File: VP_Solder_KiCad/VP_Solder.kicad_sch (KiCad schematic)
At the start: 159 parts, among them J1 Conn_01x04, SW1 SW_Push, SW2 SW_Push, U1 STM32F072CBTx, U2 XC6206PxxxMR, U3 USBLC6-2SC6

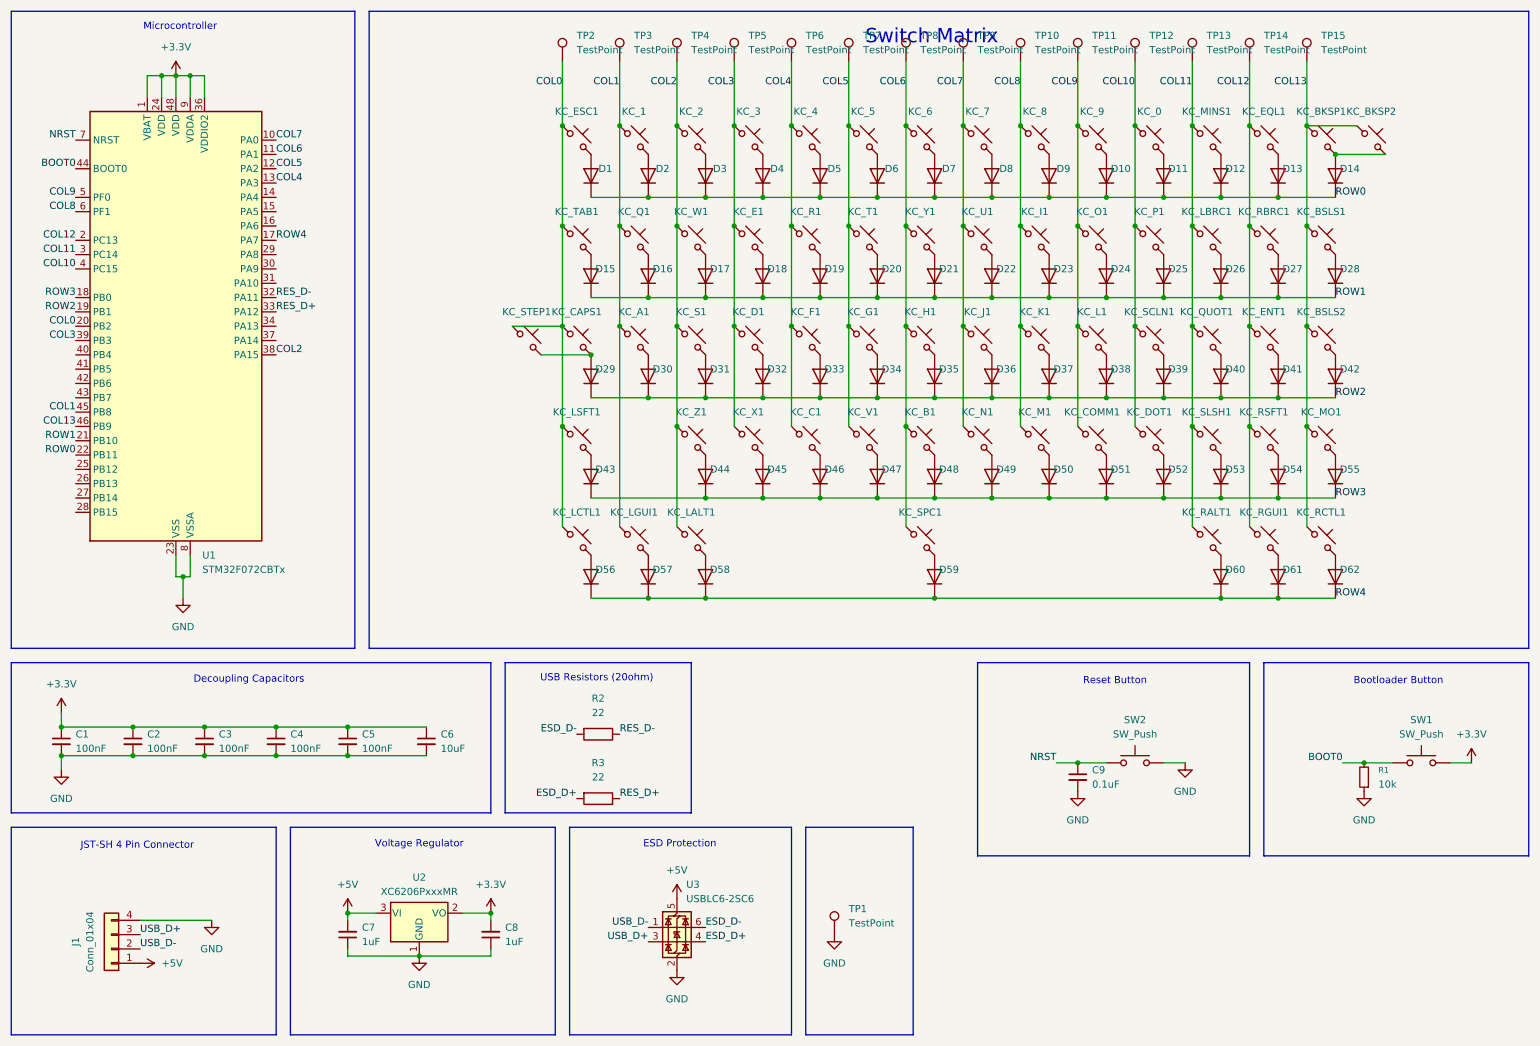
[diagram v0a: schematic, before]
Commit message: Changed testpoint names
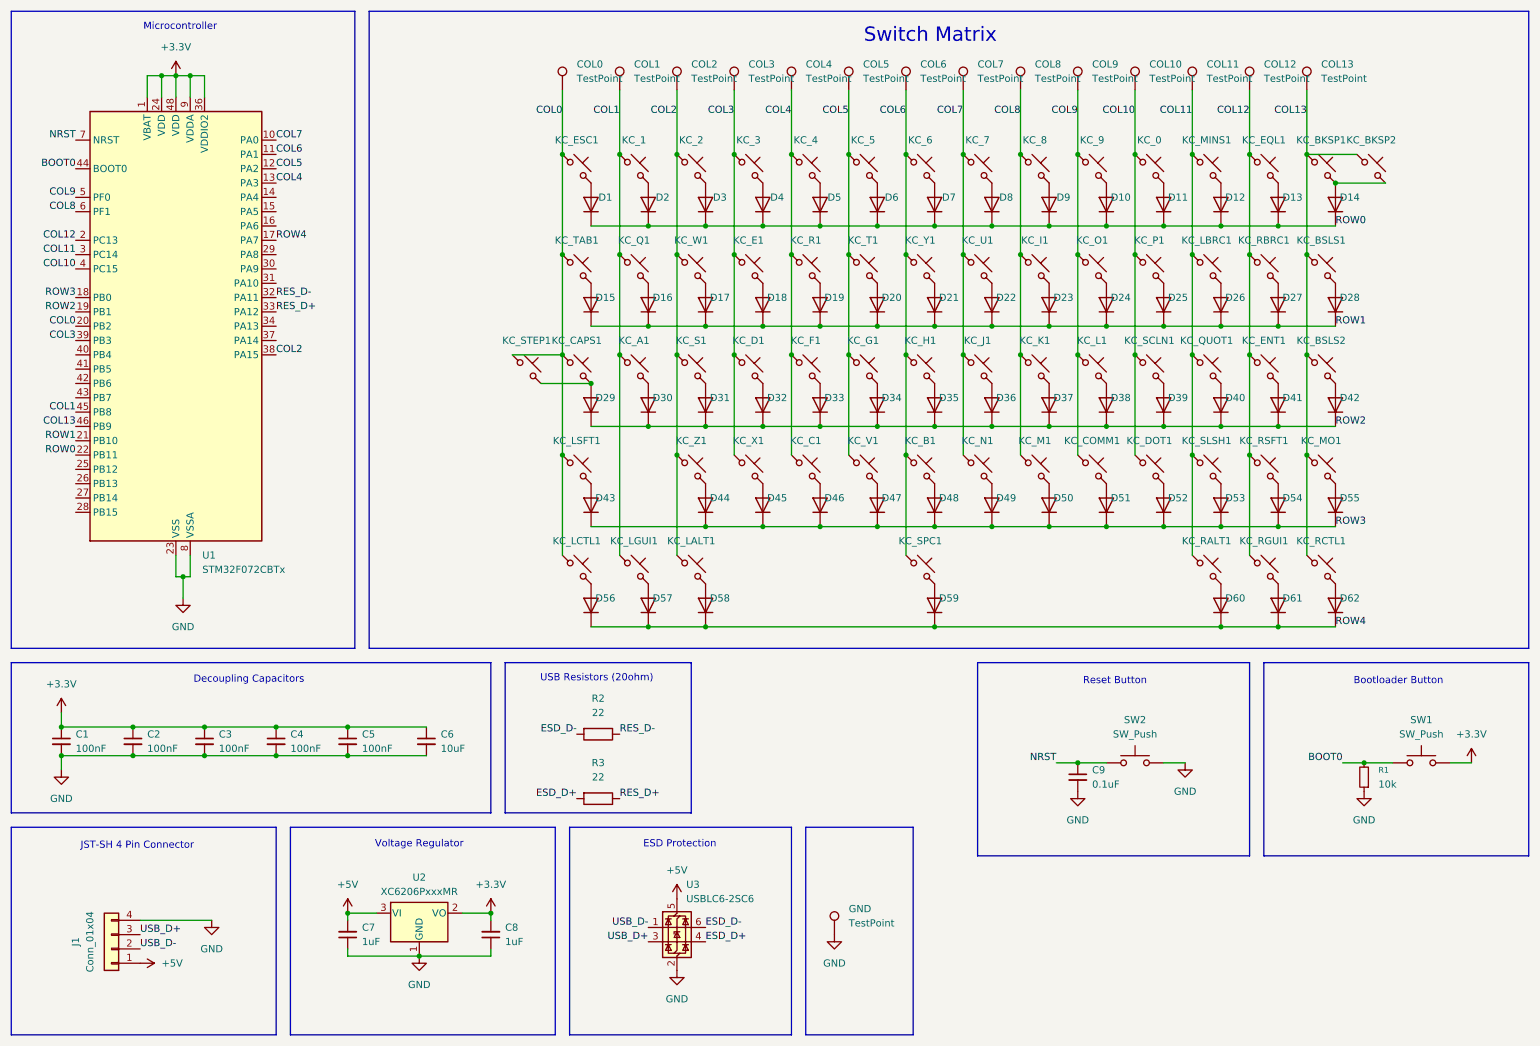
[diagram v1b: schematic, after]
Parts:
- renumbered TP2 to COL0, TP3 to COL1, TP12 to COL10, TP13 to COL11, TP14 to COL12, TP15 to COL13, TP4 to COL2, TP5 to COL3, TP6 to COL4, TP7 to COL5, TP8 to COL6, TP9 to COL7, TP10 to COL8, TP11 to COL9, TP1 to GND
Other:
- moved on the sheet: COL0, COL1, COL10, COL11, COL12, COL13, COL2, COL3, COL4, COL5, COL6, COL7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

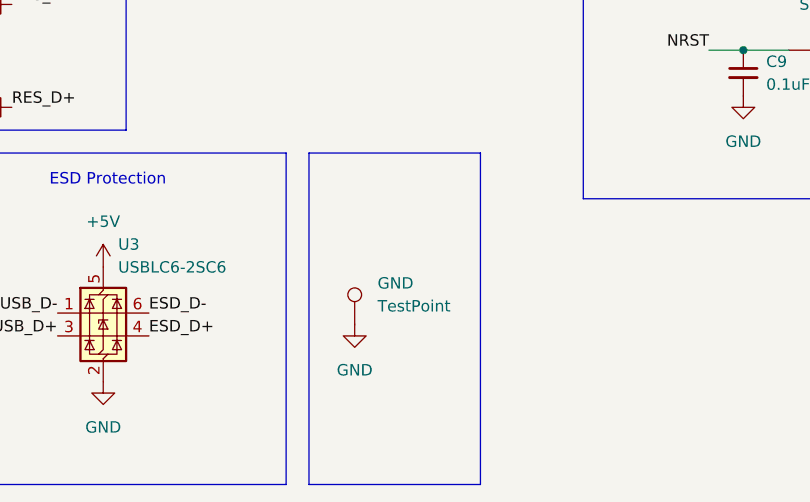
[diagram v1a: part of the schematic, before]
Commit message: Changed silkscreen
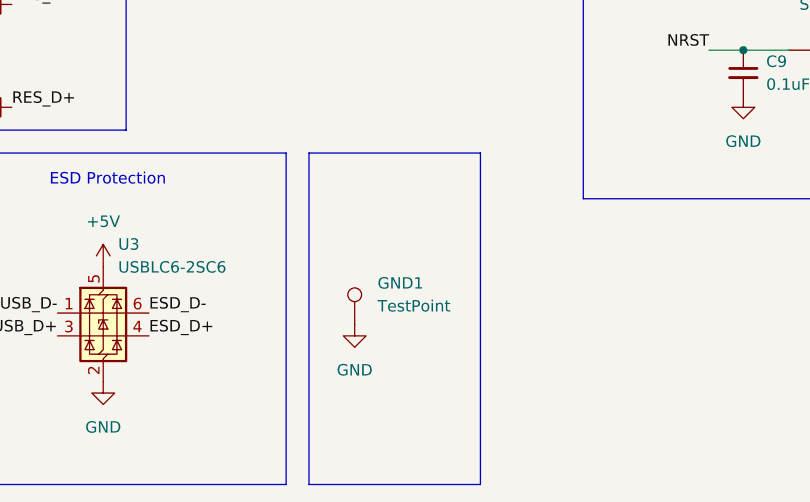
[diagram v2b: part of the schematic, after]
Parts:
- renumbered GND to GND1
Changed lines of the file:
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@@
 		(dnp no)
 		(fields_autoplaced yes)
-		(property "Reference" "GND"
+		(property "Reference" "GND1"
 			(at 162.56 173.2279 0)
 			(show_name no)
@@
 			(project "VP_Solder"
 				(path "/e464f1d1-4c01-4fad-a203-20008a0f30b7"
-					(reference "GND")
+					(reference "GND1")
 					(unit 1)
 				)

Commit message: final changes, drc fixes
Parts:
- removed R2, R3: 22, Resistor_SMD:R_0201_0603Metric, symbol Device:R
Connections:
- net RES_D+ is gone; now on net ESD_D+: U1.33 (PA12)
- net RES_D- is gone; now on net ESD_D-: U1.32 (PA11)
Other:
- note removed: "USB Resistors (20ohm)"
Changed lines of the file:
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@@
 	)
 	(rectangle
-		(start 101.6 129.54)
-		(end 134.62 156.21)
-		(stroke
-			(width 0)
-			(type default)
-		)
-		(fill
-			(type none)
-		)
-	)
-	(rectangle
 		(start 113.03 158.75)
 		(end 152.4 195.58)
@@
 		)
 	)
-	(text "USB Resistors (20ohm)"
-		(exclude_from_sim no)
-		(at 117.856 132.334 0)
-		(effects
-			(font
-				(size 1.27 1.27)
-			)
-		)
-	)
 	(junction
 		(at 147.32 69.85)
@@
 		)
 	)
-	(label "ESD_D+"
-		(at 114.3 153.67 180)
+	(label "ESD_D-"
+		(at 60.96 64.77 0)
 		(effects
 			(font
 				(size 1.27 1.27)
 			)
-			(justify right bottom)
+			(justify left bottom)
 		)
 	)
@@
 		)
 	)
-	(label "RES_D-"
-		(at 121.92 142.24 0)
-		(effects
-			(font
-				(size 1.27 1.27)
-			)
-			(justify left bottom)
-		)
-	)
 	(label "COL10"
 		(at 25.4 59.69 180)
@@
 		)
 	)
-	(label "ESD_D-"
-		(at 114.3 142.24 180)
-		(effects
-			(font
-				(size 1.27 1.27)
-			)
-			(justify right bottom)
-		)
-	)
 	(label "ROW2"
 		(at 248.92 87.63 0)
@@
 		)
 	)
-	(label "RES_D+"
-		(at 60.96 67.31 0)
-		(effects
-			(font
-				(size 1.27 1.27)
-			)
-			(justify left bottom)
-		)
-	)
 	(label "COL12"
 		(at 25.4 54.61 180)
@@
 		)
 	)
-	(label "RES_D+"
-		(at 121.92 153.67 0)
-		(effects
-			(font
-				(size 1.27 1.27)
-			)
-			(justify left bottom)
-		)
-	)
 	(label "ROW3"
 		(at 248.92 105.41 0)
@@
 		)
 	)
-	(label "RES_D-"
-		(at 60.96 64.77 0)
+	(label "ESD_D+"
+		(at 60.96 67.31 0)
 		(effects
 			(font
@@
 	)
 	(symbol
-		(lib_id "Device:R")
-		(at 118.11 153.67 270)
-		(unit 1)
-		(body_style 1)
-		(exclude_from_sim no)
-		(in_bom yes)
-		(on_board yes)
-		(in_pos_files yes)
-		(dnp no)
-		(fields_autoplaced yes)
-		(property "Reference" "R3"
-			(at 118.11 147.32 90)
-			(show_name no)
-			(do_not_autoplace no)
-			(effects
-				(font
-					(size 1.27 1.27)
-				)
-			)
-		)
-		(property "Value" "22"
-			(at 118.11 149.86 90)
-			(show_name no)
-			(do_not_autoplace no)
-			(effects
-				(font
-					(size 1.27 1.27)
-				)
-			)
-		)
-		(property "Footprint" "Resistor_SMD:R_0201_0603Metric"
-			(at 118.11 151.892 90)
-			(hide yes)
-			(show_name no)
-			(do_not_autoplace no)
-			(effects
-				(font
-					(size 1.27 1.27)
-				)
-			)
-		)
-		(property "Datasheet" ""
-			(at 118.11 153.67 0)
-			(hide yes)
-			(show_name no)
-			(do_not_autoplace no)
-			(effects
-				(font
-					(size 1.27 1.27)
-				)
-			)
-		)
-		(property "Description" "Resistor"
-			(at 118.11 153.67 0)
-			(hide yes)
-			(show_name no)
-			(do_not_autoplace no)
-			(effects
-				(font
-					(size 1.27 1.27)
-				)
-			)
-		)
-		(pin "1"
-		)
-		(pin "2"
-		)
-		(instances
-			(project "VP_Solder"
-				(path "/e464f1d1-4c01-4fad-a203-20008a0f30b7"
-					(reference "R3")
-					(unit 1)
-				)
-			)
-		)
-	)
-	(symbol
 		(lib_id "Switch:SW_Push")
 		(at 213.36 147.32 0)
@@
 					(unit 1)
 				)
-			)
-		)
-	)
-	(symbol
-		(lib_id "Device:R")
-		(at 118.11 142.24 270)
-		(unit 1)
-		(body_style 1)
-		(exclude_from_sim no)
-		(in_bom yes)
-		(on_board yes)
-		(in_pos_files yes)
-		(dnp no)
-		(fields_autoplaced yes)
-		(property "Reference" "R2"
-			(at 118.11 135.89 90)
-			(show_name no)
-			(do_not_autoplace no)
-			(effects
-				(font
-					(size 1.27 1.27)
-				)
-			)
-		)
-		(property "Value" "22"
-			(at 118.11 138.43 90)
-			(show_name no)
-			(do_not_autoplace no)
-			(effects
-				(font
-					(size 1.27 1.27)
-				)
-			)
-		)
-		(property "Footprint" "Resistor_SMD:R_0201_0603Metric"
-			(at 118.11 140.462 90)
-			(hide yes)
-			(show_name no)
-			(do_not_autoplace no)
-			(effects
-				(font
-					(size 1.27 1.27)
-				)
-			)
-		)
-		(property "Datasheet" ""
-			(at 118.11 142.24 0)
-			(hide yes)
-			(show_name no)
-			(do_not_autoplace no)
-			(effects
-				(font
-					(size 1.27 1.27)
-				)
-			)
-		)
-		(property "Description" "Resistor"
-			(at 118.11 142.24 0)
-			(hide yes)
-			(show_name no)
-			(do_not_autoplace no)
-			(effects
-				(font
-					(size 1.27 1.27)
-				)
-			)
-		)
-		(pin "1"
-		)
-		(pin "2"
-		)
-		(instances
-			(project "VP_Solder"
-				(path "/e464f1d1-4c01-4fad-a203-20008a0f30b7"
-					(reference "R2")
-					(unit 1)
-				)
